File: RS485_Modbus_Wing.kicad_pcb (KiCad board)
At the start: 2 copper layers, 50.8 x 22.9 mm, 6 parts, among them J1 feather long, J2 feather short

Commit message: Add_netlist
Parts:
- added C1: 0.1uF, Capacitor_SMD:C_0603_1608Metric, F.Cu at (149.1, 106.9)
- added R1: 1K, Resistor_SMD:R_0603_1608Metric_Pad1.05x0.95mm_HandSolder, F.Cu at (123.8, 115.0)
- added R2: 4.7K, Resistor_SMD:R_0805_2012Metric_Pad1.15x1.40mm_HandSolder, F.Cu at (146.1, 101.2)
- added R3: 4.7K, Resistor_SMD:R_0805_2012Metric_Pad1.15x1.40mm_HandSolder, F.Cu at (146.1, 104.2)
- added R4: 1K, Resistor_SMD:R_0603_1608Metric_Pad1.05x0.95mm_HandSolder, F.Cu at (128.2, 115.0)
- added R5: 4.7K, Resistor_SMD:R_0805_2012Metric_Pad1.15x1.40mm_HandSolder, F.Cu at (144.7, 109.1)
- added R6: 120R, Resistor_SMD:R_0603_1608Metric_Pad1.05x0.95mm_HandSolder, F.Cu at (144.5, 111.8)
- added R7: 1K, Resistor_SMD:R_0603_1608Metric_Pad1.05x0.95mm_HandSolder, F.Cu at (144.5, 114.4)
- added R8: 1K, Resistor_SMD:R_0603_1608Metric_Pad1.05x0.95mm_HandSolder, F.Cu at (148.9, 111.8)
- added U1: VOS617A, Package_SO:SO-4_4.4x2.3mm_P1.27mm, F.Cu at (138.8, 101.7)
- added U2: MAX13487E, Package_SO:SOIC-8_3.9x4.9mm_P1.27mm, F.Cu at (138.1, 110.9)
- added U3: VOS617A, Package_SO:SO-4_4.4x2.3mm_P1.27mm, F.Cu at (138.8, 105.7)
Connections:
- net /F0 renamed /D0
- net /F1 renamed /D1
- net /F2 renamed /D2
- net /F3 renamed /D3
- net /F4 renamed /D4
- net /F5 renamed /D5
- net /F6 renamed /D6

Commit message: Fist_PCB
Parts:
- added J3: Screw_Terminal_01x02, TerminalBlock:TerminalBlock_Altech_AK300-2_P5.00mm, F.Cu at (167.5, 82.9)
- moved R1 48.8 mm to (158.0, 80.2)
- moved R4 42.0 mm to (151.2, 79.9), turned to 180 degrees
- moved R7 34.6 mm to (147.8, 79.9), turned to 180 degrees
- moved R8 30.5 mm to (140.0, 82.7), turned to 90 degrees
- moved R6 26.4 mm to (158.7, 89.5), turned to 90 degrees
- moved U1 25.3 mm to (155.2, 82.5)
- moved U3 24.3 mm to (146.0, 82.4)
- moved U2 23.4 mm to (147.1, 89.2)
- moved C1 19.8 mm to (152.2, 87.4), turned to 270 degrees
- moved R3 19.0 mm to (156.0, 87.9), turned to 180 degrees
- moved R5 18.3 mm to (142.0, 91.0), turned to 270 degrees
- moved R2 13.9 mm to (156.1, 91.6)
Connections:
- J2 pad 10: /VUSB -> VBUS
- J2 pad 3: /D0 -> /D0RX
- J2 pad 4: /D1 -> /D1TX
- R7 pad 2: Net-(R7-Pad2) -> /DI
- U3 pad 4: Net-(R7-Pad2) -> /DI
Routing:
- net VBUS: track 0.00 -> 47.9 mm, vias 0 -> 1
- net +3V3: track 0.00 -> 42.6 mm
- net /B: track 0.00 -> 24.7 mm
- net /A: track 0.00 -> 24.2 mm
- net /D1TX: track 0.00 -> 22.8 mm
- net /DI: track 0.00 -> 21.5 mm
- net GND: track 0.00 -> 12.1 mm, vias 0 -> 3
- net /RO: track 0.00 -> 11.8 mm
- net /D0RX: track 0.00 -> 9.58 mm
- net Net-(R5-Pad1): track 0.00 -> 4.17 mm
- net Net-(R8-Pad2): track 0.00 -> 2.85 mm
- net Net-(R4-Pad1): track 0.00 -> 1.99 mm
- added copper zone on B.Cu, net GND
- added copper zone on F.Cu, net GND
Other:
- net class Default: trace_width 0.25 -> 0.3
- net class Source added: clearance 0.25, trace_width 0.5, via_dia 0.8, via_drill 0.4

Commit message: Add_Logo
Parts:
- added G***: LOGO, Aesthetics:electronic_cats_logo_8x6, F.Cu at (127.9, 85.5)
- added G***: LOGO, Aesthetics:bast_8x8, B.Cu at (131.2, 85.0)
- J3: footprint TerminalBlock:TerminalBlock_Altech_AK300-2_P5.00mm -> TerminalBlock:TerminalBlock_bornier-2_P5.08mm
- moved J3 2.62 mm to (170.1, 83.4)
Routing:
- net /B: track 24.7 -> 27.1 mm
- net /A: track 24.2 -> 24.9 mm
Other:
- board text added: "D0"
- board text added: "D1"
- board text added: "D2"
- board text added: "D3"
- board text added: "D4"
- board text added: "D5"
- board text added: "D6"
- board text added: "VBUS"
- board text removed: "F0"
- board text removed: "F1"
- board text removed: "F2"
- board text removed: "F3"
- board text removed: "F4"
- board text removed: "F5"
- board text removed: "F6"
- board text removed: "VUSB"

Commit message: Last_Revision
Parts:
- moved G*** 4.72 mm to (132.6, 85.2)
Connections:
- J2 pad 3: /D0RX -> /D0
- J2 pad 4: /D1TX -> /D1
- R1 pad 2: /D0RX -> /RX
- U1 pad 4: /D0RX -> /RX
- U3 pad 2: /D1TX -> /TX
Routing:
- net /TX: track 0.00 -> 37.8 mm
- net /D1TX: track 22.8 -> 0.00 mm
- net /RX: track 0.00 -> 19.2 mm, vias 0 -> 1
- net +3V3: track 42.6 -> 53.2 mm
- net /D0RX: track 9.58 -> 0.00 mm
- net /B: track 27.1 -> 28.5 mm
- net VBUS: track 47.9 -> 47.1 mm
- net GND: track 12.1 -> 12.3 mm, vias 3 -> 4
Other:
- board text added: "NC"
- board text added: "RS485_Modbus_Wing"
- board text removed: "FREE"

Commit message: change_pin
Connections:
- net /D2 renamed /D9
- net /D3 renamed /D10
- net /D4 renamed /D11
- J2 pad 3: /D0 -> /D5
- J2 pad 4: /D1 -> /D6
- J2 pad 8: /D5 -> /D12
- J2 pad 9: /D6 -> /D13
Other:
- board text added: "D10"
- board text added: "D11"
- board text added: "D12"
- board text added: "D13"
- board text added: "D9"
- board text added: "MI"
- board text added: "MO"
- board text added: "V1.0"
- board text removed: "D0"
- board text removed: "D1"
- board text removed: "D2"
- board text removed: "D3"
- board text removed: "D4"
- board text removed: "MISO"
- board text removed: "MOSI"

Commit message: Add_Label
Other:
- board text added: "A"
- board text added: "B"
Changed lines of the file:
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@@
   (general
     (thickness 1.6)
-    (drawings 38)
+    (drawings 40)
     (tracks 141)
     (zones 0)
@@
     )
   )
+  (gr_text A (at 165.63 88.5) (layer F.SilkS)
+    (effects (font (size 1 1) (thickness 0.15)))
+  )
+  (gr_text B (at 165.64 83.5) (layer F.SilkS)
+    (effects (font (size 1 1) (thickness 0.15)))
+  )
   (gr_text V1.0 (at 126.69 85.48 270) (layer F.SilkS)

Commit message: ChangeRS
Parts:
- removed R8: 1K, Resistor_SMD:R_0603_1608Metric_Pad1.05x0.95mm_HandSolder
- removed U2: MAX13487E, Package_SO:SOIC-8_3.9x4.9mm_P1.27mm
- removed U3: VOS617A, Package_SO:SO-4_4.4x2.3mm_P1.27mm
- added C2: 0.1uF, Capacitor_SMD:C_0603_1608Metric_Pad1.05x0.95mm_HandSolder, F.Cu at (141.3, 84.4)
- C1: value 0.1uF -> 10uF; footprint Capacitor_SMD:C_0603_1608Metric -> Capacitor_SMD:C_0603_1608Metric_Pad1.05x0.95mm_HandSolder
- R1, R4: value 1K -> 10K
- R2, R3: value 4.7K -> 10K; footprint Resistor_SMD:R_0805_2012Metric_Pad1.15x1.40mm_HandSolder -> Resistor_SMD:R_0603_1608Metric_Pad1.05x0.95mm_HandSolder
- R5: value 4.7K -> 20K; footprint Resistor_SMD:R_0805_2012Metric_Pad1.15x1.40mm_HandSolder -> Resistor_SMD:R_0603_1608Metric_Pad1.05x0.95mm_HandSolder
- R6: value 120R -> 120
- R7: value 1K -> 20K
- U1: value VOS617A -> SP3485EN; footprint Package_SO:SO-4_4.4x2.3mm_P1.27mm -> Package_SO:SOIC-8_3.9x4.9mm_P1.27mm
- moved R5 13.5 mm to (155.4, 89.2), turned to 180 degrees
- moved C1 10.9 mm to (141.3, 87.8), turned to 90 degrees
- moved R7 9.41 mm to (149.0, 89.2)
- moved R3 8.40 mm to (148.2, 85.0), turned to 90 degrees
- moved R6 6.75 mm to (152.1, 91.1), turned to 180 degrees
- moved R2 6.67 mm to (157.0, 85.0), turned to 270 degrees
- moved R4 3.46 mm to (148.2, 81.6), turned to 90 degrees
- moved U1 3.09 mm to (152.2, 83.2), turned to 270 degrees
- moved R1 1.77 mm to (157.0, 81.6), turned to 90 degrees
- moved J3 0.15 mm to (170.1, 83.3)
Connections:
- C1 pad 1: VBUS -> +3V3
- J2 pad 10: VBUS -> /VBUS
- J2 pad 5: /D9 -> /RO
- J2 pad 6: /D10 -> /RE
- J2 pad 7: /D11 -> /DE
- J2 pad 8: /D12 -> /DI
- J3 pad 1: /B -> /RS485B
- J3 pad 2: /A -> /RS485A
- R1 pad 2: /RX -> /RO
- R2 pad 1: /A -> +3V3
- R2 pad 2: VBUS -> /RE
- R3 pad 1: GND -> +3V3
- R3 pad 2: /B -> /DE
- R4 pad 1: Net-(R4-Pad1) -> +3V3
- R4 pad 2: VBUS -> /DI
- R5 pad 1: Net-(R5-Pad1) -> GND
- R5 pad 2: VBUS -> /RS485B
- R6 pad 1: /A -> /RS485B
- R6 pad 2: /B -> /RS485A
- R7 pad 1: VBUS -> /RS485A
- R7 pad 2: /DI -> +3V3
- U1 pad 1: Net-(R4-Pad1) -> /RO
- U1 pad 2: /RO -> /RE
- U1 pad 3: GND -> /DE
- U1 pad 4: /RX -> /DI
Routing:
- net VBUS: track 47.1 -> 0.00 mm, vias 1 -> 0
- net /TX: track 37.8 -> 0.00 mm
- net /RS485B: track 0.00 -> 31.2 mm
- net /RS485A: track 0.00 -> 28.5 mm
- net /B: track 28.5 -> 0.00 mm
- net /A: track 24.9 -> 0.00 mm
- net /RX: track 19.2 -> 0.00 mm, vias 1 -> 0
- net /RE: track 0.00 -> 14.5 mm
- net /DI: track 21.5 -> 7.59 mm
- net /DE: track 0.00 -> 12.0 mm
- net GND: track 12.3 -> 17.9 mm
- net Net-(R5-Pad1): track 4.17 -> 0.00 mm
- net /RO: track 11.8 -> 8.40 mm
- net +3V3: track 53.2 -> 56.3 mm
- net Net-(R8-Pad2): track 2.85 -> 0.00 mm
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
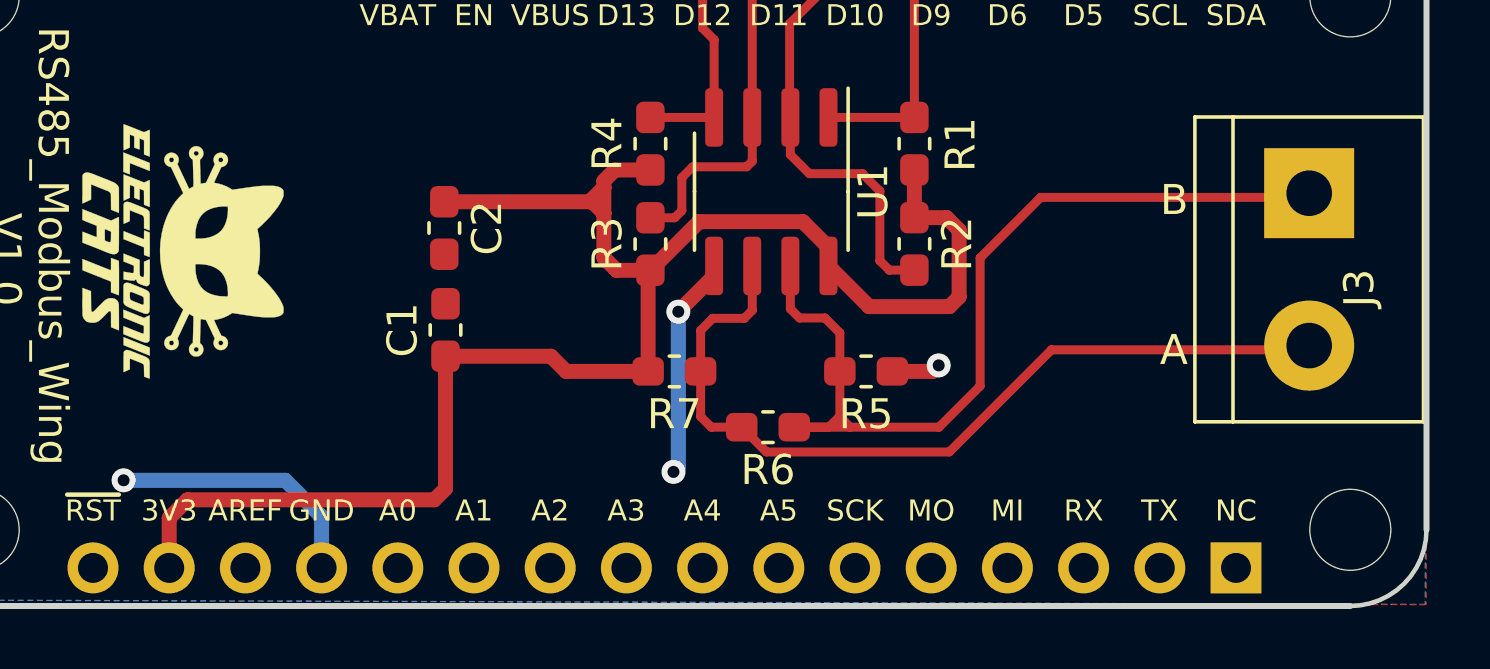
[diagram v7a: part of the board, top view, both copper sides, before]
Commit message: Move_capacitor
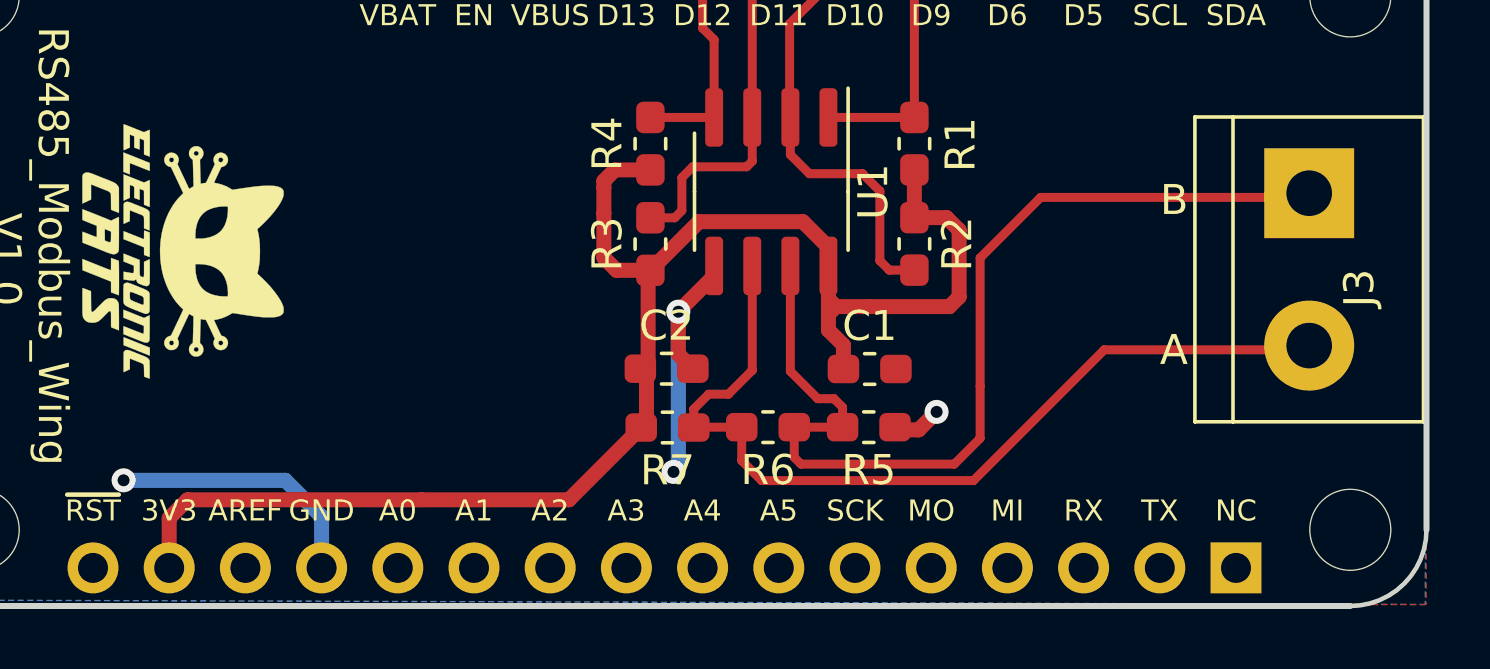
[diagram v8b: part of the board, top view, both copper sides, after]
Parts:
- moved C1 14.2 mm to (155.5, 89.1), turned to 0 degrees
- moved C2 8.77 mm to (148.7, 89.1), turned to 0 degrees
- moved R7 1.88 mm to (148.8, 91.1)
- moved R5 1.86 mm to (155.5, 91.1)
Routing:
- net +3V3: track 56.3 -> 52.9 mm
- net /RS485B: track 31.2 -> 33.4 mm
- net GND: track 17.9 -> 19.9 mm
- net /RS485A: track 28.5 -> 30.2 mm
